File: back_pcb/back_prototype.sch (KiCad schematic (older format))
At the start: 80 parts, among them P1 EXPANSION_LEFT, P10 CONN_01X08, P2 EXPANSION_BOTTOM, P3 EXPANSION_TOP, P4 USB_A, P5 AUDIO_CONN, P6 ATMEGA_HEADER, P7 EXPANSION_BOTTOM2, P8 JST, P9 USB_A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

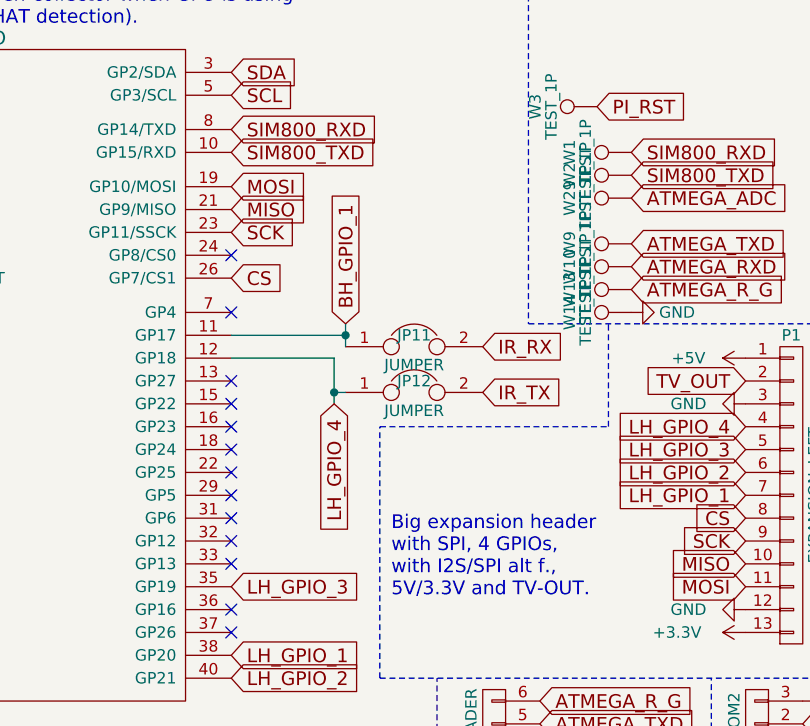
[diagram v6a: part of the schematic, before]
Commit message: Started using GPIO4 for IR TX
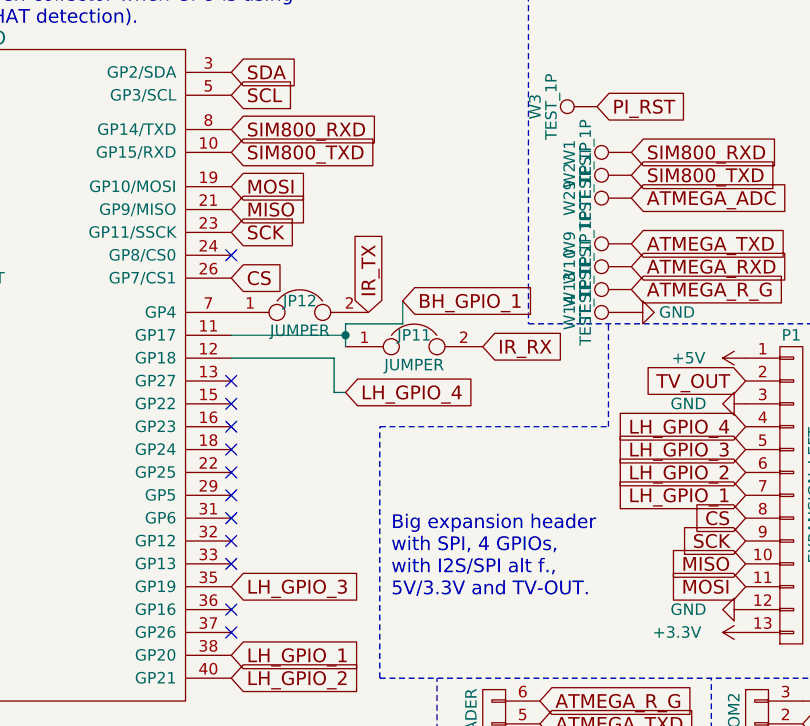
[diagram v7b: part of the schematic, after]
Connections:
- net LH_GPIO_4: no longer JP12.1
- net at U1.7 (GP4): now also JP12.1
- no-connect marks 26 -> 25
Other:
- moved on the sheet: JP12
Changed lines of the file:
@@
 	0    1    1    0
 $EndComp
-Text GLabel 3550 5400 2    60   Input ~ 0
+Text GLabel 3050 5050 1    60   Input ~ 0
 IR_TX
 $Comp
@@
 L JUMPER JP12
 U 1 1 58C70E5F
-P 3250 5400
-F 0 "JP12" H 3250 5450 50  0000 C CNN
-F 1 "JUMPER" H 3250 5320 50  0000 C CNN
-F 2 "common-footprints:GS2_SMALL" H 3250 5400 50  0001 C CNN
-F 3 "" H 3250 5400 50  0000 C CNN
-	1    3250 5400
+P 2750 5050
+F 0 "JP12" H 2750 5100 50  0000 C CNN
+F 1 "JUMPER" H 2750 4970 50  0000 C CNN
+F 2 "common-footprints:GS2_SMALL" H 2750 5050 50  0001 C CNN
+F 3 "" H 2750 5050 50  0000 C CNN
+	1    2750 5050
 	1    0    0    -1
 $EndComp
@@
 Wire Wire Line
 	2450 5250 2900 5250
-Wire Wire Line
-	2900 5250 2900 5450
-Wire Wire Line
-	2900 5400 2950 5400
 Connection ~ 3800 7250
 Wire Wire Line
@@
 Connection ~ 1900 7450
 Connection ~ 1900 7250
-NoConn ~ 2450 5050
 Connection ~ 1000 7250
 Connection ~ 1000 7450
@@
 Wire Wire Line
 	2950 5100 2950 5200
-Text GLabel 2950 5100 1    60   Input ~ 0
+Text GLabel 3200 5000 2    60   Input ~ 0
 BH_GPIO_1
 $Comp
@@
 Wire Notes Line
 	4550 7500 6950 7500
-Connection ~ 2900 5400
 Text GLabel 6600 6850 0    60   Input ~ 0
 BH_GPIO_1
-Text GLabel 2900 5450 3    60   Input ~ 0
+Text GLabel 2950 5400 2    60   Input ~ 0
 LH_GPIO_4
 Connection ~ 2950 5150
@@
 Wire Wire Line
 	10450 2800 10750 2800
+Wire Wire Line
+	2950 5400 2900 5400
+Wire Wire Line
+	2900 5400 2900 5250
+Wire Wire Line
+	2950 5100 3200 5100
+Wire Wire Line
+	3200 5100 3200 5000
 $EndSCHEMATC

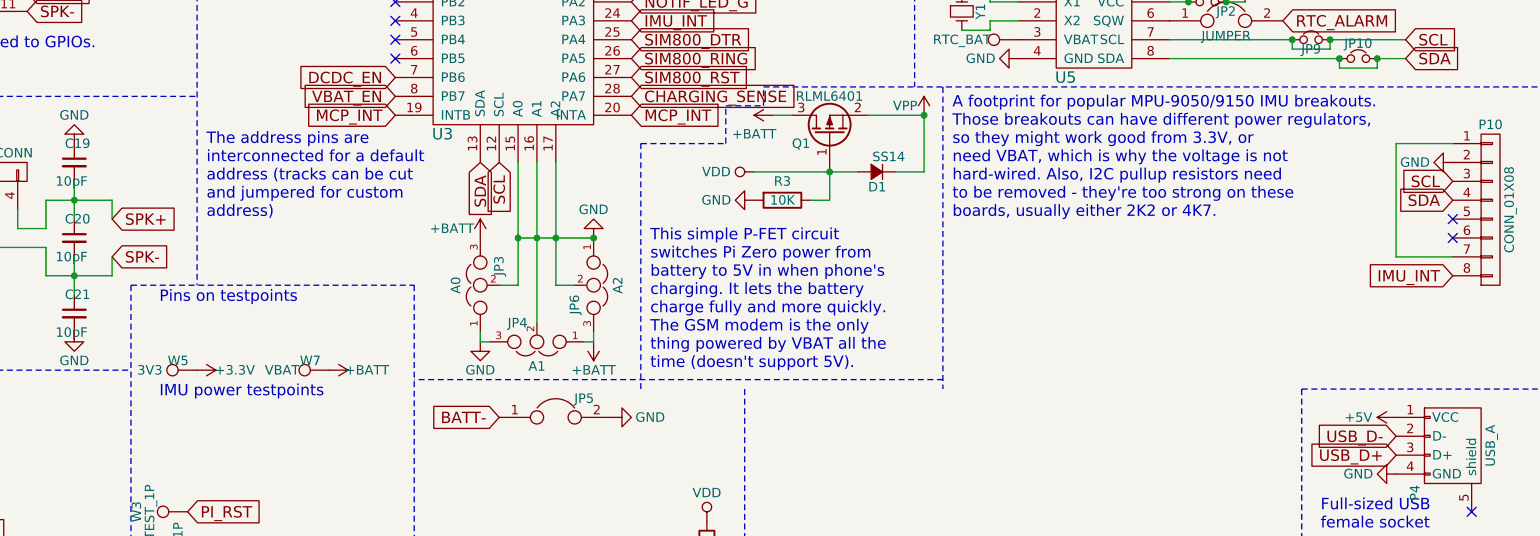
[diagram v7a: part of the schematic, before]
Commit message: Fixed protection footprint
More like "fucked shit up because Chinese modules"
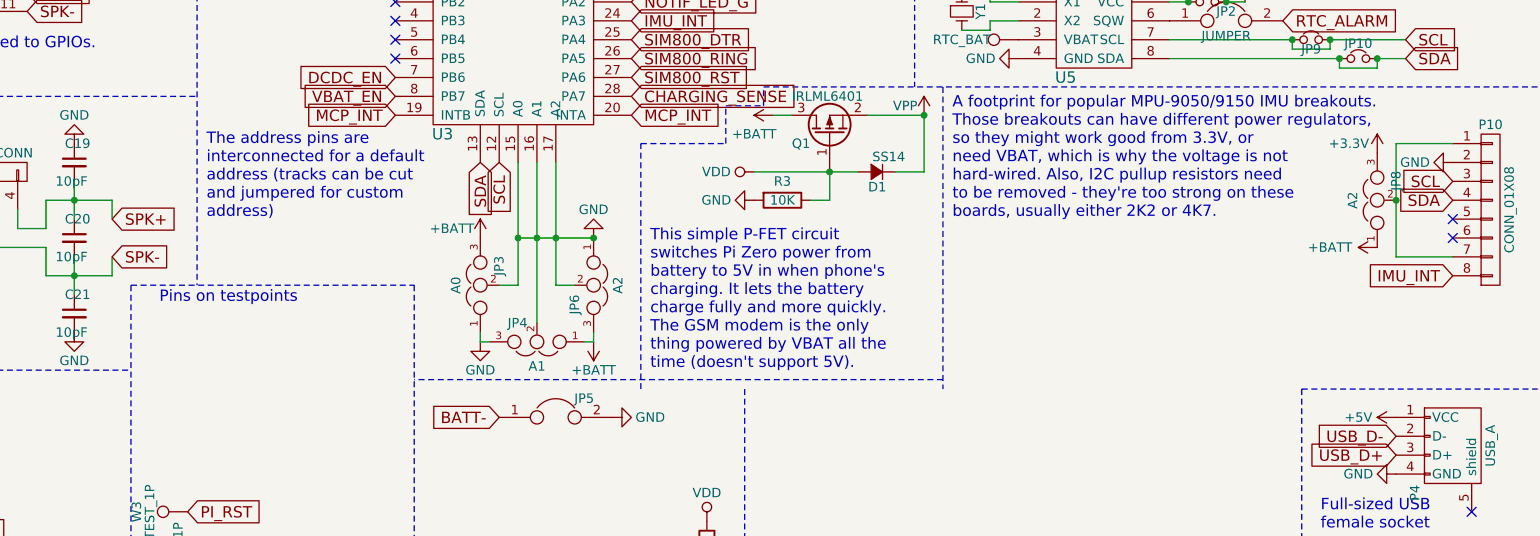
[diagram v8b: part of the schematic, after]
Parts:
- removed W5: 3V3, Measurement_Points:Measurement_Point_Square-SMD-Pad_Small, symbol TEST_1P
- removed W7: VBAT, Measurement_Points:Measurement_Point_Square-SMD-Pad_Small, symbol TEST_1P
- added JP8: A2, common-footprints:GS3_SMALL, symbol JUMPER3
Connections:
- net +3V3: now also JP8.3
- net +BATT: now also JP8.1
- net at P10.1 (P1), P10.7 (P7): now also JP8.2
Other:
- note removed: "IMU power testpoints"
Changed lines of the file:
@@
-	0    1    1    0
-$EndComp
-Text Notes 3900 3550 0    60   ~ 0
-IMU power testpoints
-$Comp
-L TEST_1P W5
-U 1 1 5909549F
-P 4100 3400
-F 0 "W5" V 4150 3500 50  0000 C CNN
-F 1 "3V3" V 4100 3650 50  0000 C CNN
-F 2 "Measurement_Points:Measurement_Point_Square-SMD-Pad_Small" H 4300 3400 50  0001 C CNN
-F 3 "" H 4300 3400 50  0000 C CNN
-	1    4100 3400
-	0    -1   -1   0
-$EndComp
-$Comp
-L TEST_1P W7
-U 1 1 59095B40
-P 4800 3400
-F 0 "W7" V 4850 3500 50  0000 C CNN
-F 1 "VBAT" V 4800 3650 50  0000 C CNN
-F 2 "Measurement_Points:Measurement_Point_Square-SMD-Pad_Small" H 5000 3400 50  0001 C CNN
-F 3 "" H 5000 3400 50  0000 C CNN
-	1    4800 3400
-	0    -1   -1   0
-$EndComp
-$Comp
-L +BATT #PWR072
-U 1 1 59095E15
-P 4800 3400
-F 0 "#PWR072" H 4800 3250 50  0001 C CNN
-F 1 "+BATT" V 4800 3600 50  0000 C CNN
-F 2 "" H 4800 3400 50  0000 C CNN
-F 3 "" H 4800 3400 50  0000 C CNN
-	1    4800 3400
-	0    1    1    0
-$EndComp
-$Comp
-L +3.3V #PWR073
-U 1 1 59096AA8
-P 4100 3400
-F 0 "#PWR073" H 4100 3250 50  0001 C CNN
-F 1 "+3.3V" V 4100 3600 50  0000 C CNN
-F 2 "" H 4100 3400 50  0000 C CNN
-F 3 "" H 4100 3400 50  0000 C CNN
-	1    4100 3400
 	0    1    1    0
 $EndComp
@@
 $EndComp
 $Comp
-L GND #PWR074
+L GND #PWR072
 U 1 1 590944F1
 P 7300 5450
-F 0 "#PWR074" H 7300 5200 50  0001 C CNN
+F 0 "#PWR072" H 7300 5200 50  0001 C CNN
 F 1 "GND" V 7400 5350 50  0000 C CNN
 F 2 "" H 7300 5450 50  0000 C CNN
@@
 Wire Wire Line
 	3200 5100 3200 5000
+$Comp
+L JUMPER3 JP8
+U 1 1 590A25CF
+P 10350 2500
+F 0 "JP8" H 10400 2400 50  0000 L CNN
+F 1 "A2" H 10350 2600 50  0000 C BNN
+F 2 "common-footprints:GS3_SMALL" H 10350 2500 50  0001 C CNN
+F 3 "" H 10350 2500 50  0000 C CNN
+	1    10350 2500
+	0    -1   -1   0
+$EndComp
+$Comp
+L +BATT #PWR073
+U 1 1 590A31F3
+P 10350 2750
+F 0 "#PWR073" H 10350 2600 50  0001 C CNN
+F 1 "+BATT" V 10350 3000 50  0000 C CNN
+F 2 "" H 10350 2750 50  0000 C CNN
+F 3 "" H 10350 2750 50  0000 C CNN
+	1    10350 2750
+	0    -1   -1   0
+$EndComp
+$Comp
+L +3.3V #PWR074
+U 1 1 590A3C9E
+P 10350 2250
+F 0 "#PWR074" H 10350 2100 50  0001 C CNN
+F 1 "+3.3V" H 10200 2300 50  0000 C CNN
+F 2 "" H 10350 2250 50  0000 C CNN
+F 3 "" H 10350 2250 50  0000 C CNN
+	1    10350 2250
+	1    0    0    -1
+$EndComp
+Connection ~ 10450 2500
 $EndSCHEMATC
